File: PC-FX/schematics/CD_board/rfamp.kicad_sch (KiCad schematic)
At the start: 18 parts, among them CN101 Conn_01x18_Socket, IC101 CXA1610M, Q101 PNP

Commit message: Schematics pretty much done. Expect some mistakes but it captures enough information to help understanding its behaviour.
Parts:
- removed R456: 1k, symbol Device:R
- added C104, C106: ?, symbol Device:C
- added C105, C107: 10uF, Capacitor_SMD:CP_Elec_5x5.4, symbol Device:C_Polarized
- added C313: 100uF, Capacitor_SMD:CP_Elec_5x5.4, symbol Device:C_Polarized
- added R101: 15, symbol Device:R
- added R103: 20k, symbol Device:R
- added R107: 4k7, symbol Device:R
- added R108: 51k, symbol Device:R
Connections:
- net GND: now also C101.2, C103.2, C104.2, C105.2, C313.2
- net RFO: now also R103.1, R107.2
- net VC: now also C105.1, C106.2, C107.2, C313.1
- net ~{LDON}: now also IC101.19 (~{LDON}), R112.2
- net at C101.1: now also CN101.6 (Pin_6), R101.1
- net RFI: no longer names the net of IC101.17 (RFI)
- net RFI: now also R103.2, R108.1
- net VCC renamed +5V
- net +5V: now also C104.1, C107.1, R101.2; no longer CN101.6 (Pin_6)
- new net: C106.1, R107.1, R108.2
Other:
- note removed: "IC104 P17"
- note removed: "IC104 P18"
- note removed: "IC104 P26"
- note removed: "IC104 P27"
- title: PC FX Pots Adfustment Schematics -> PC-FX CD Board Schematics
- moved on the sheet: C101, C103, R104, R105, R109, R112, R118, VR101, VR102

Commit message: Confirmed connections and fixed issues on Servo and DSP chips using similar design - Sony CDP-790
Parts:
- Q101: symbol Simulation_SPICE:PNP -> Device:Q_PNP_BCE
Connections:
- net at Q101.1 (B): now also C102.2, IC101.1 (LD); no longer L101.2
- new net: L101.2, Q101.2 (C)
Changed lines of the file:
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@@
 	)
 	(symbol
-		(lib_id "Simulation_SPICE:PNP")
+		(lib_id "Device:Q_PNP_BCE")
 		(at 113.03 74.93 180)
 		(unit 1)
@@
 		(fields_autoplaced yes)
 		(property "Reference" "Q101"
-			(at 108.1786 73.7179 0)
+			(at 108.1786 73.7178 0)
 			(effects
 				(font
@@
 		)
 		(property "Footprint" ""
-			(at 77.47 74.93 0)
+			(at 107.95 77.47 0)
 			(effects
 				(font
@@
 			)
 		)
-		(property "Datasheet" "https://ngspice.sourceforge.io/docs/ngspice-html-manual/manual.xhtml#cha_BJTs"
-			(at 77.47 74.93 0)
+		(property "Datasheet" "~"
+			(at 113.03 74.93 0)
 			(effects
 				(font
@@
 			)
 		)
-		(property "Description" "Bipolar transistor symbol for simulation only, substrate tied to the emitter"
+		(property "Description" "PNP transistor, base/collector/emitter"
 			(at 113.03 74.93 0)
 			(effects

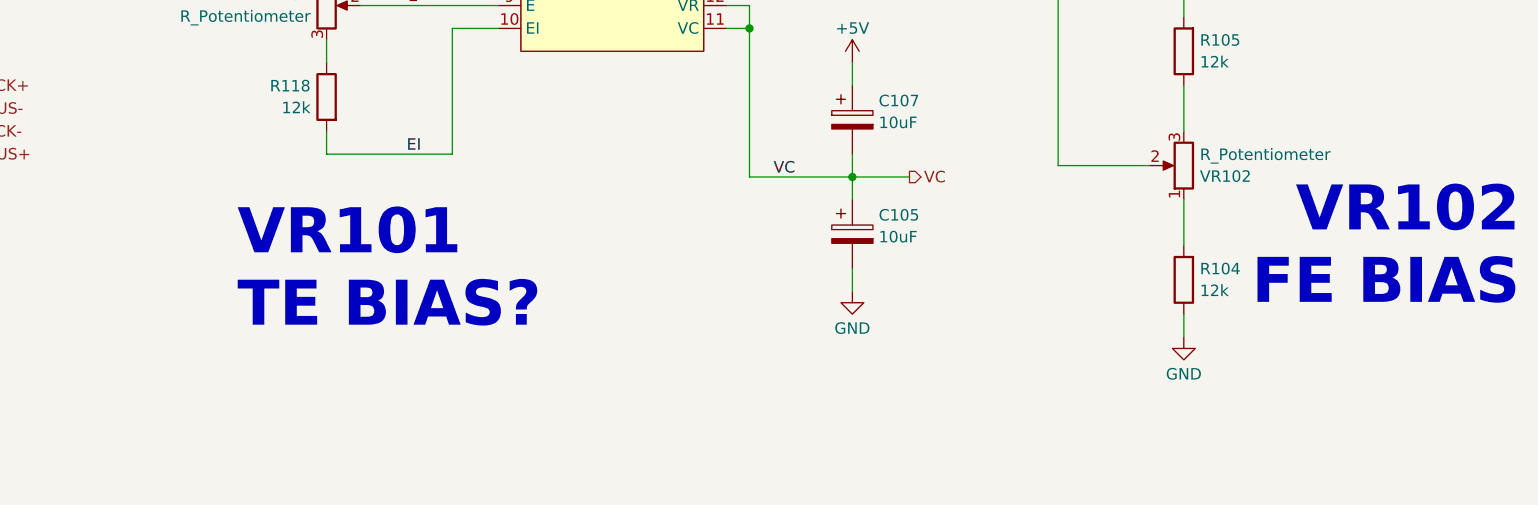
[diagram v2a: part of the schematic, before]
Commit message: Small update based on confirmation of SCSI control signals
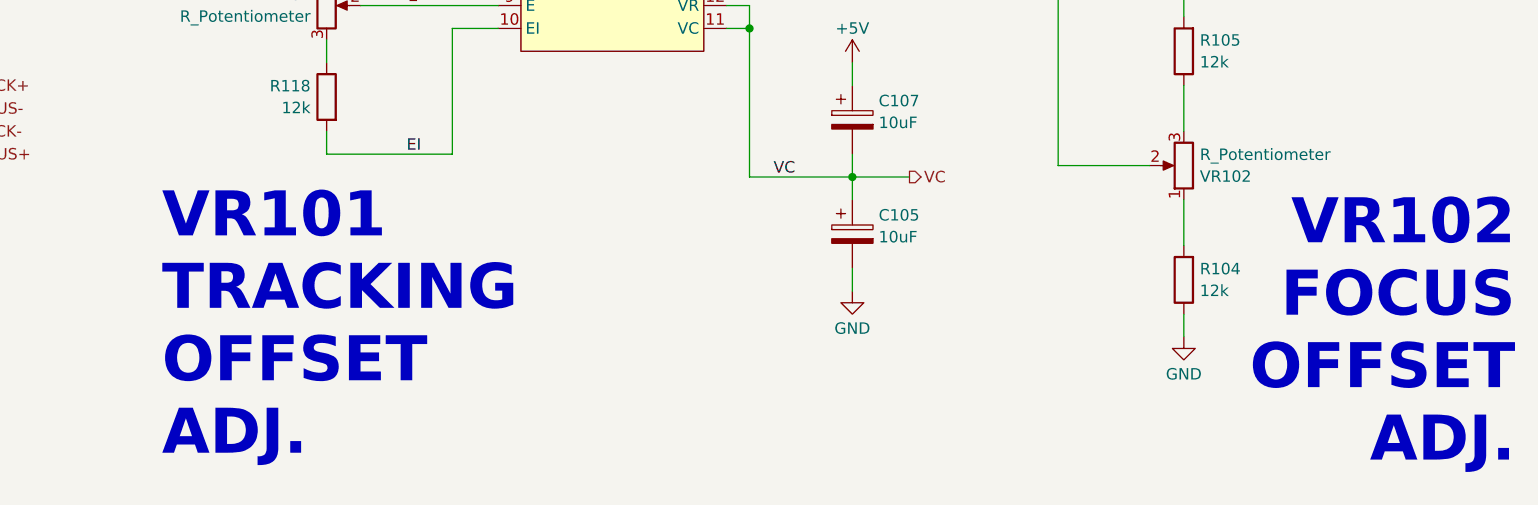
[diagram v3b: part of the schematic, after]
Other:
- note added: "VR101 TRACKING OFFSET ADJ."
- note added: "VR102 FOCUS OFFSET ADJ."
- note removed: "VR101 TE BIAS?"
- note removed: "VR102 FE BIAS"
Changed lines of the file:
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@@
 		)
 	)
-	(text "VR102\nFE BIAS"
+	(text "VR102\nFOCUS\nOFFSET\nADJ."
 		(exclude_from_sim no)
-		(at 265.938 143.002 0)
+		(at 265.43 160.528 0)
 		(effects
 			(font
@@
 		)
 	)
-	(text "VR101\nTE BIAS?"
+	(text "VR101\nTRACKING\nOFFSET\nADJ."
 		(exclude_from_sim no)
-		(at 123.444 145.542 0)
+		(at 115.062 159.766 0)
 		(effects
 			(font
